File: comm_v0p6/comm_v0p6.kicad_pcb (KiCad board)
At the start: 4 copper layers, 40 x 40 mm, 12 parts, among them J1 1x15 header, J2 1x15 socket, J4 2x2 socket, J5 2x2 socket, J6 2x2 socket, J7 2x2 socket, U1 ATmega328PB-M, Y1 20MHz

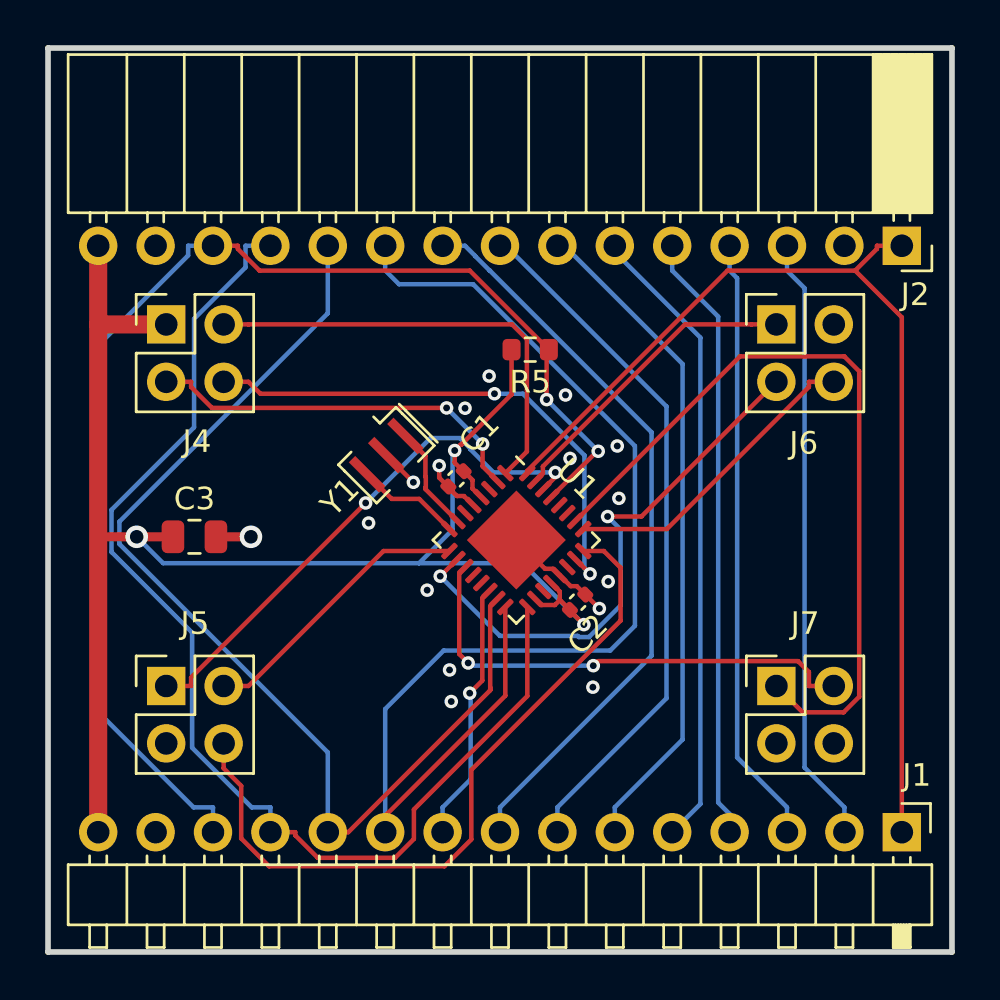
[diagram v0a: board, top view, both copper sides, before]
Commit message: Worked on comm_v0p6 routing.
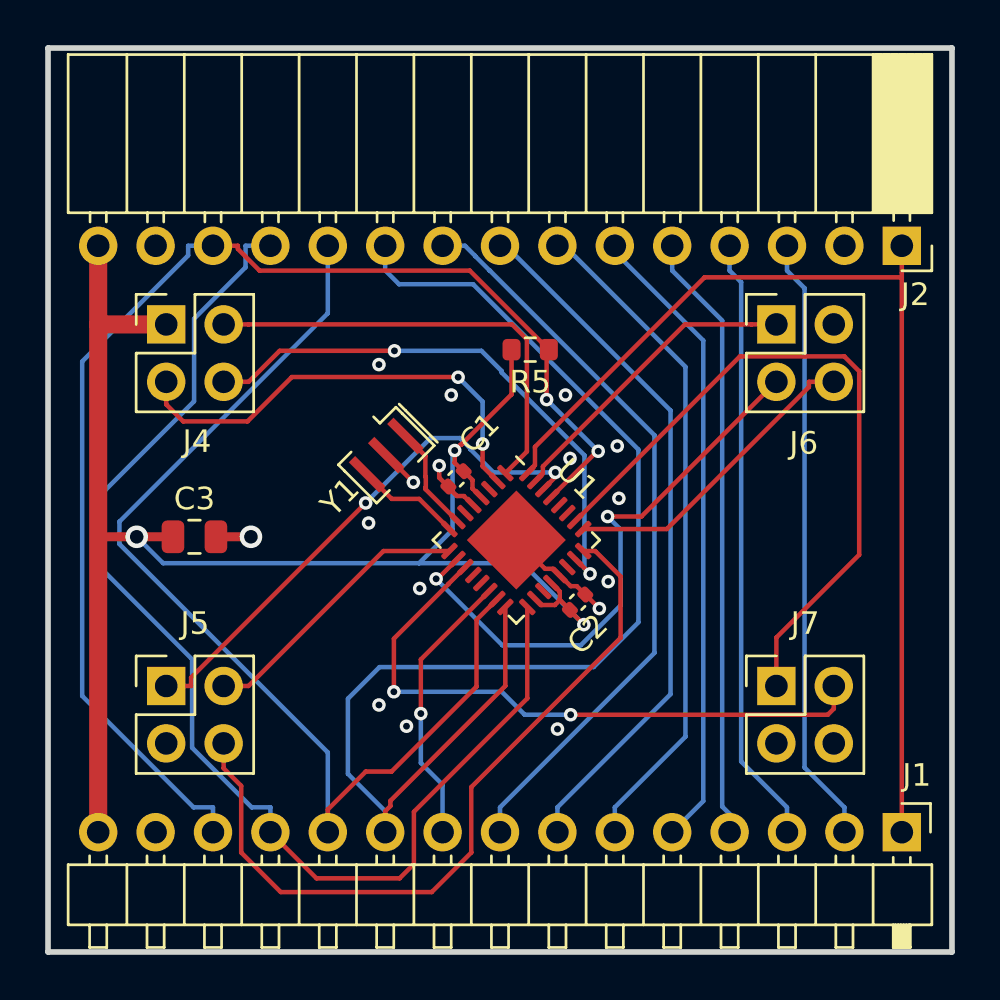
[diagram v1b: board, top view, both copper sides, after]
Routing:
- net /B1_CS3: track 21.7 -> 27.8 mm
- net /RESET_DRV3: track 34.7 -> 31.3 mm
- net /B1_SCK: track 17.2 -> 20.4 mm
- net /B0_MISO: track 53.5 -> 56.6 mm
- net /B0_SCK: track 52.5 -> 54.2 mm
- net /RESET_DRV1: track 32.4 -> 33.9 mm
- net /RESET_DRV0: track 23.6 -> 24.8 mm
- net /RESET_MSTR: track 56.4 -> 57.1 mm
- net /B0_CS0: track 11.6 -> 12.3 mm
- net /B1_CS2: track 24.9 -> 25.5 mm
